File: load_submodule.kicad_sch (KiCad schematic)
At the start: 8 parts, among them Q1 RFP30N06LE

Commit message: Included Shunt Values
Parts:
- added C8: 220uF, symbol Device:C_US
- added Q2: 2N2219, Package_TO_SOT_THT:TO-39-3, symbol Transistor_BJT:2N2219
- added R13: 220, symbol Device:R
- added R14: 470, symbol Device:R
- added R15, R16: R, symbol Device:R
- added R17: 10, symbol Device:R
- added RE1: Relay, symbol windTurbineSchemSymLib:Relay
- added U1, U2: INA229AQDGSRQ1, VSSOP10_DGS_TEX, symbol INA229:INA229AQDGSRQ1
- C5: value C_US -> 100uF
- C6: value C_US -> 22uF
- C7: value C_US -> 220uF
- L1, L2: value L -> 150u
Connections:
- net Converter_Out: now also RE1.5 (COM)
- net GND: now also BT1.2 (-), C8.2, Q2.1 (E), R17.2, RE1.3 (GND), U1.7 (GND), U2.7 (GND)
- net MCU: now also R14.1
- net Rectifier+: now also R16.1, U2.10 (IN+), U2.8 (VBUS); no longer C5.1, L1.1
- net at BT1.1 (+): now also R15.2, U1.9 (IN)
- new net: Q2.3 (C), R13.2, RE1.2 (IN)
- new net: Q2.2 (B), R14.2
- new net: R15.1, RE1.6 (NO), U1.10 (IN+)
- new net +3.3V: C8.1, U1.6 (VS), U2.6 (VS)
- new net +5V: R13.1, RE1.1 (Vcc)
- new net Battery+: U1.8 (VBUS)
- new net Battery_Alert: U1.3 (ALERT)
- new net Battery_CS: U1.1 (CS)
- new net Battery_MISO: U1.4 (MISO)
- new net Battery_MOSI: U1.2 (MOSI)
- new net Battery_SCLK: U1.5 (SCLK)
- new net Converter_In: C5.1, L1.1, R16.2, U2.9 (IN)
- new net Dump_Load: R17.1, RE1.4 (NC)
- new net Rectifier_ALERT: U2.3 (ALERT)
- new net Rectifier_CS: U2.1 (CS)
- new net Rectifier_MISO: U2.4 (MISO)
- new net Rectifier_MOSI: U2.2 (MOSI)
- new net Rectifier_SCLK: U2.5 (SCLK)
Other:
- note added: "100kHz"
- note added: "3.3V"
- note added: "Battery_Shunt"
- note added: "Load Submodule"
- moved on the sheet: BT1, C5, C6, C7, D1, L1, L2, Q1

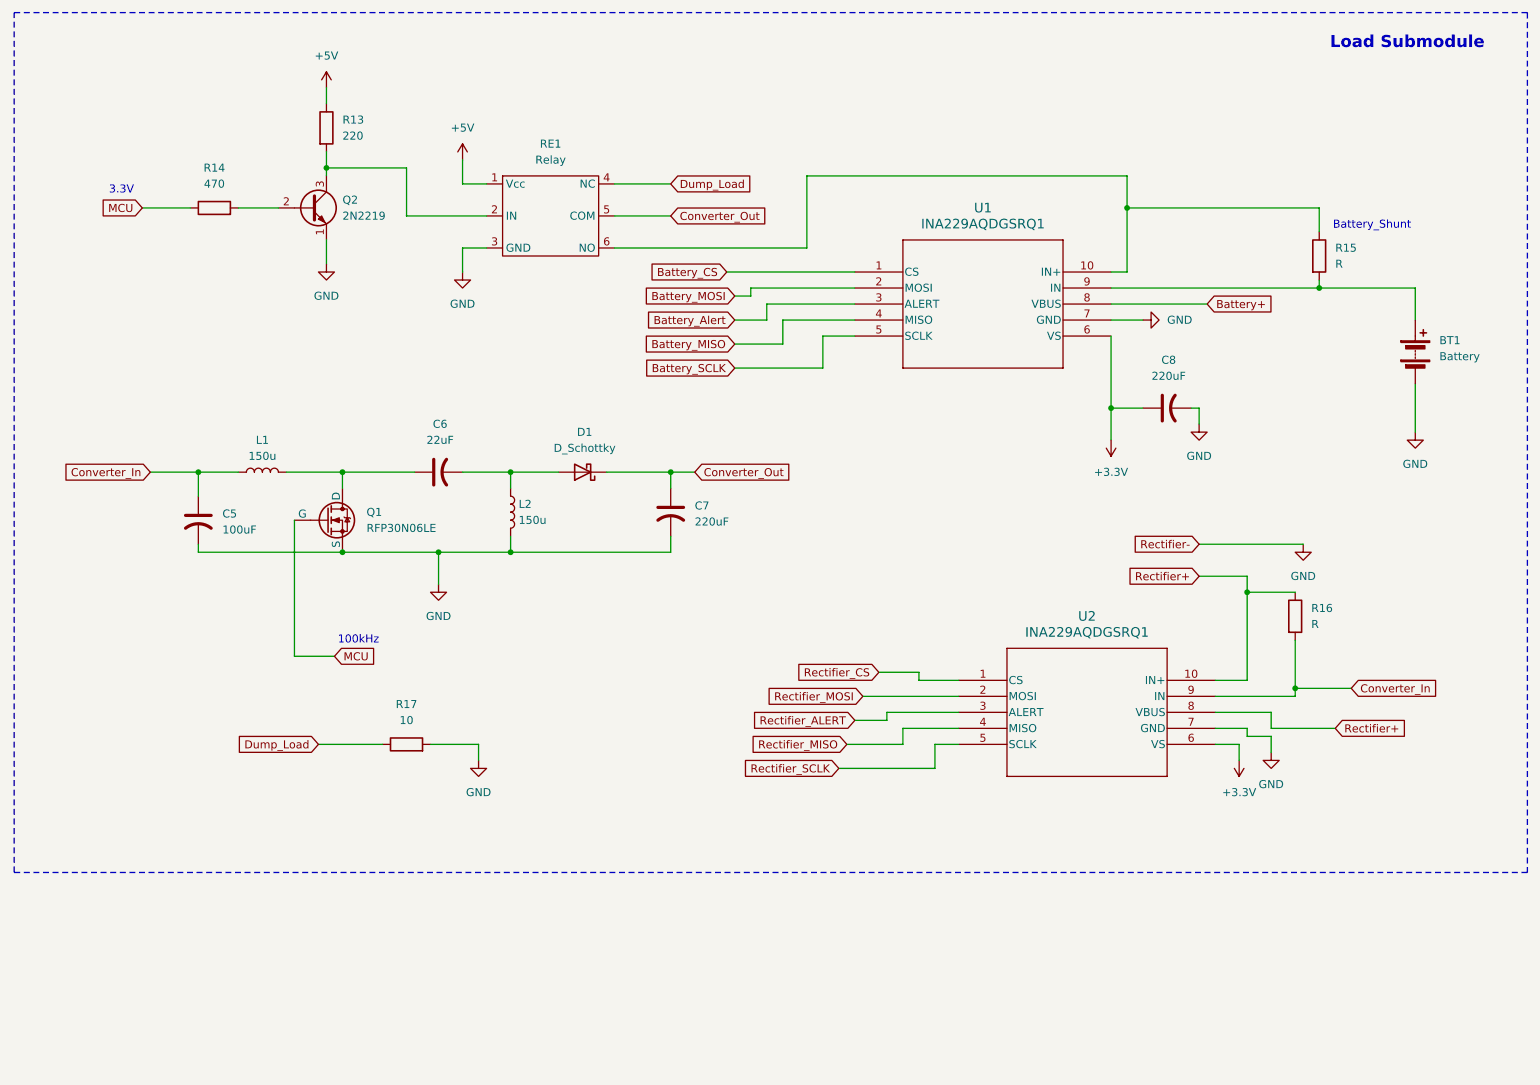
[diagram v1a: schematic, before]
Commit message: Finished Squematics V1
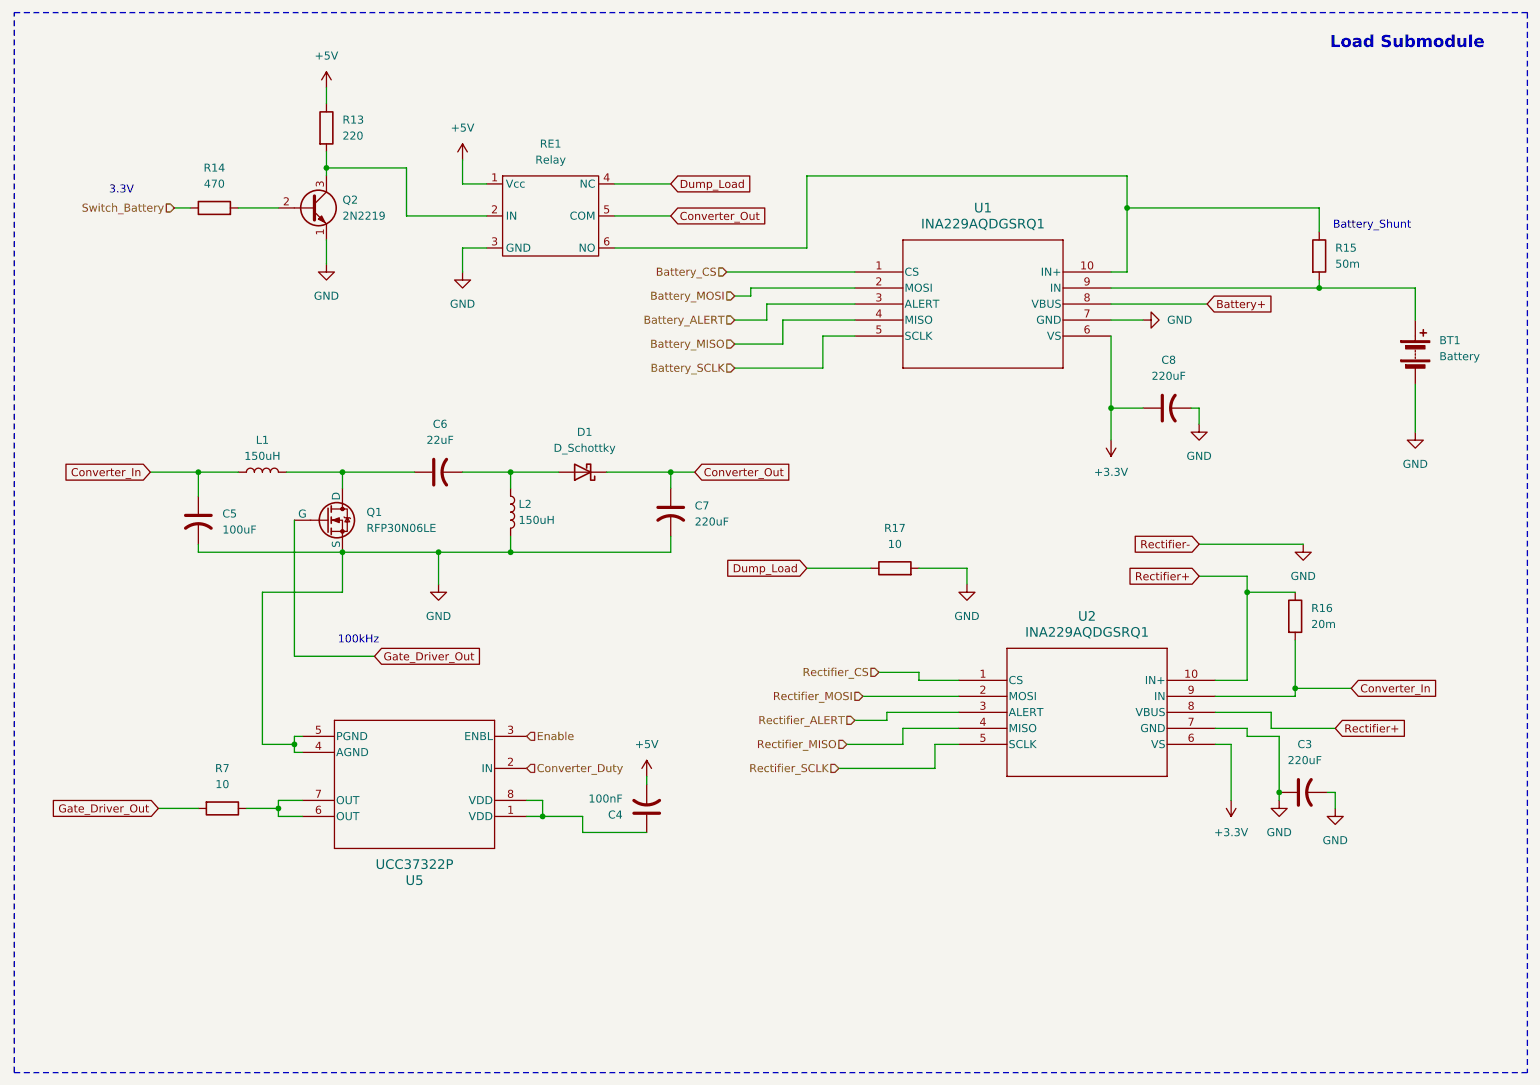
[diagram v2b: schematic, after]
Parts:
- added C3: 220uF, symbol Device:C_US
- added C4: 100nF, symbol Device:C_US
- added R7: 10, symbol Device:R
- added U5: UCC37322P, P0008A, symbol UCC32322:UCC37322P
- L1, L2: value 150u -> 150uH
- R15: value R -> 50m
- R16: value R -> 20m
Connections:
- net +5V: now also C4.2
- net GND: now also C3.1, C3.2, U5.4 (AGND), U5.5 (PGND)
- net Battery_Alert renamed Battery_ALERT
- net MCU renamed Gate_Driver_Out
- net Gate_Driver_Out: now also R7.2; no longer R14.1
- new net: R7.1, U5.6 (OUT), U5.7 (OUT)
- new net: C4.1, U5.1 (VDD), U5.8 (VDD)
- new net Converter_Duty: U5.2 (IN)
- new net Enable: U5.3 (ENBL)
- new net Switch_Battery: R14.1
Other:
- company: (none) -> PRES
- title: (none) -> Load Submodule
- moved on the sheet: R17

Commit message: Added better colors
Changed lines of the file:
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@@
 	)
 	(symbol
+		(lib_name "INA229AQDGSRQ1_1")
 		(lib_id "INA229:INA229AQDGSRQ1")
 		(at 158.75 67.31 0)

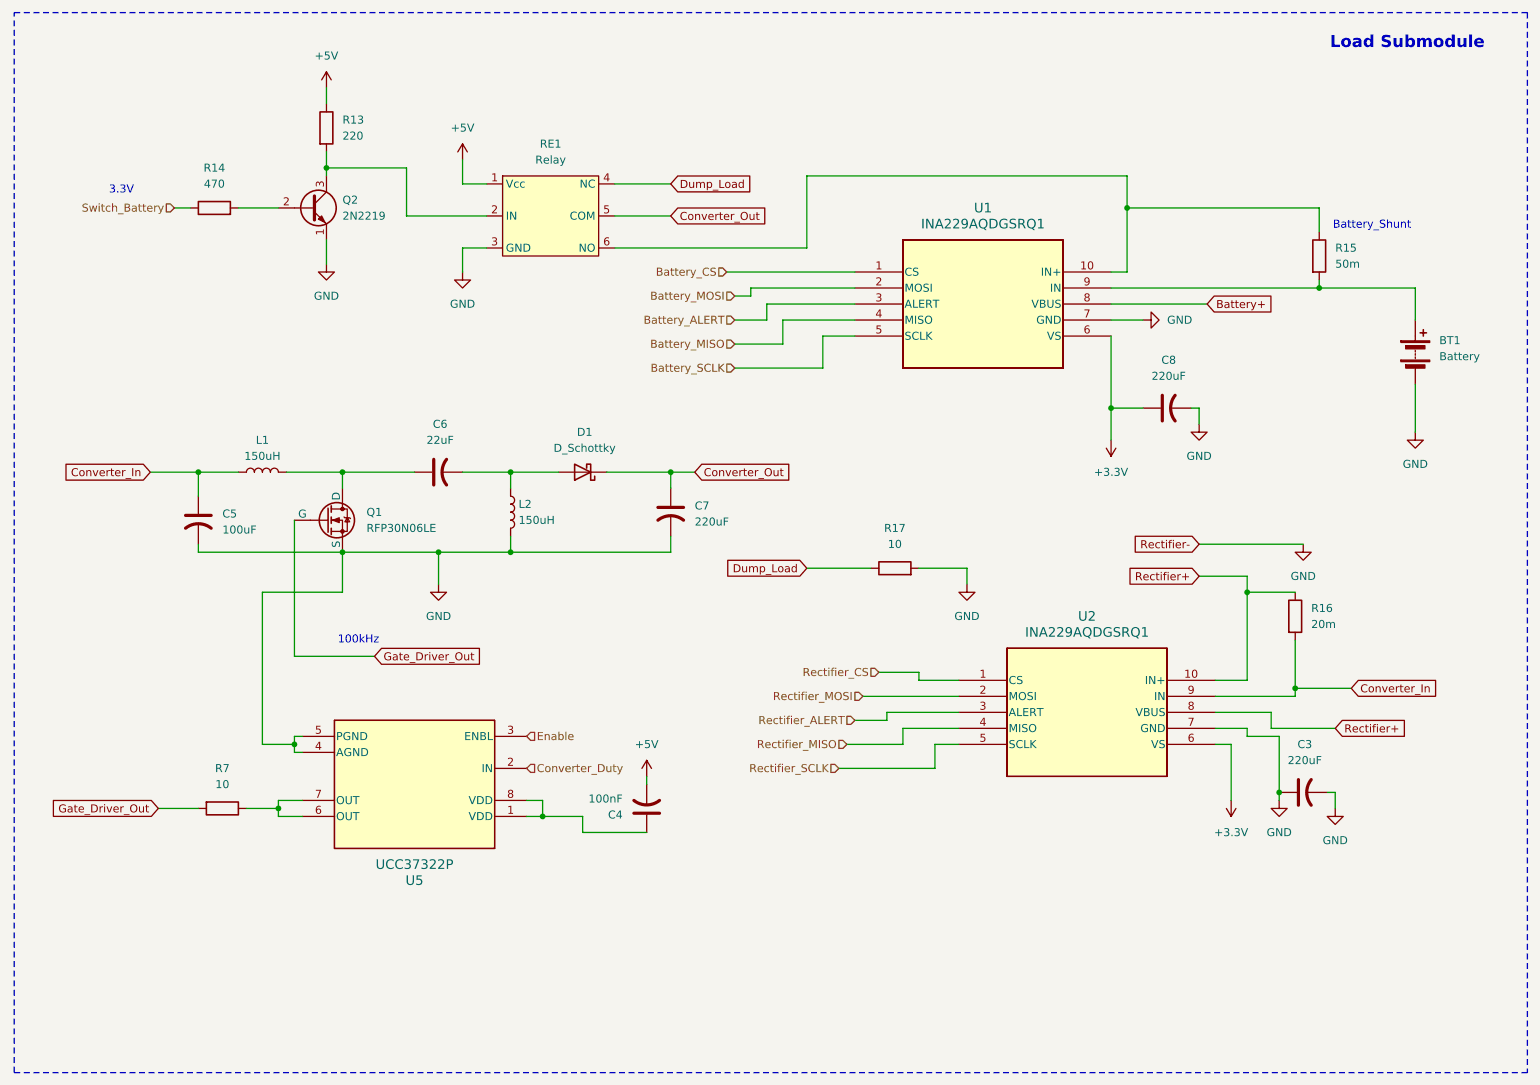
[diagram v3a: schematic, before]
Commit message: converter values adjusted
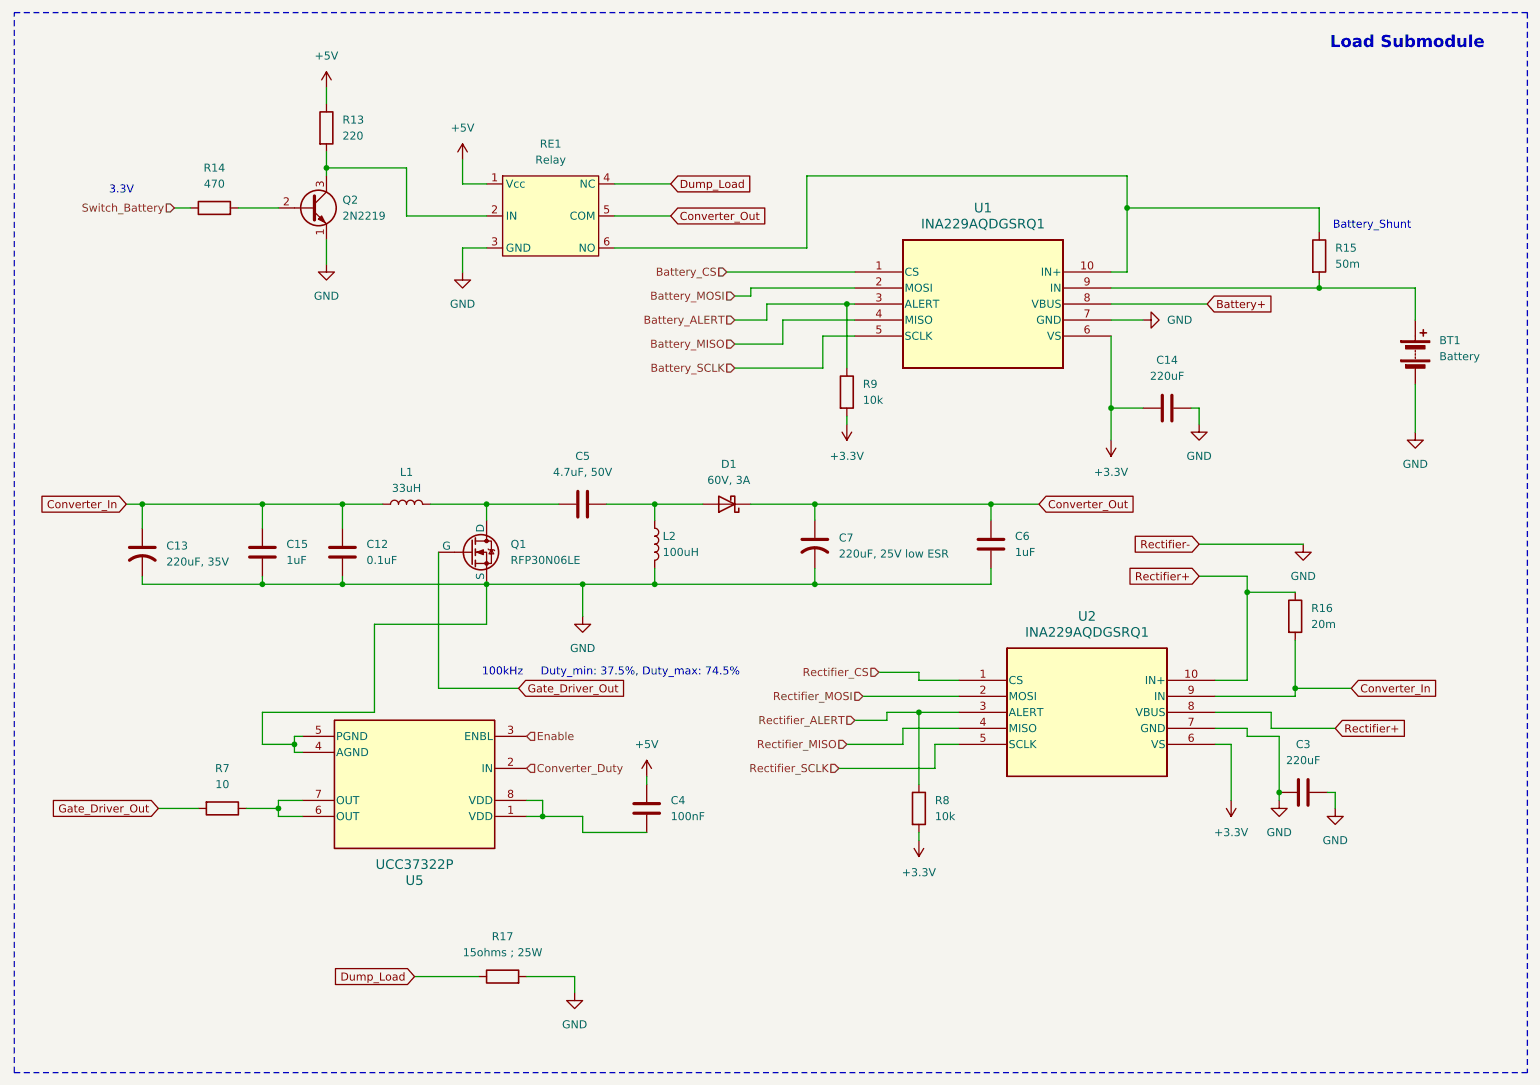
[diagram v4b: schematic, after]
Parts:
- removed C3, C8: 220uF, symbol Device:C_US
- removed C4: 100nF, symbol Device:C_US
- removed C5: 100uF, symbol Device:C_US
- removed C6: 22uF, symbol Device:C_US
- added C12: 0.1uF, symbol Device:C
- added C13: 220uF, 35V, symbol Device:C_US
- added C14, C3: 220uF, symbol Device:C
- added C15, C6: 1uF, symbol Device:C
- added C4: 100nF, symbol Device:C
- added C5: 4.7uF, 50V, symbol Device:C
- added R8, R9: 10k, symbol Device:R
- C7: value 220uF -> 220uF, 25V low ESR
- D1: value D_Schottky -> 60V, 3A
- L1: value 150uH -> 33uH
- L2: value 150uH -> 100uH
- R17: value 10 -> 15ohms ; 25W
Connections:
- net +3.3V: now also C14.1, R8.2, R9.2
- net +5V: now also C4.1
- net Battery_ALERT: now also R9.1
- net Converter_In: now also C12.1, C13.1, C15.1
- net Converter_Out: now also C6.2
- net GND: now also C12.2, C13.2, C14.2, C15.2, C3.1, C3.2, C6.1
- net Rectifier_ALERT: now also R8.1
- net at D1.2 (A), L2.1: now also C5.2
- net at L1.2, Q1.1 (D): now also C5.1
- net at U5.1 (VDD), U5.8 (VDD): now also C4.2
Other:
- note added: "Duty_min: 37.5%, Duty_max: 74.5%"
- moved on the sheet: C7, D1, L1, L2, Q1, R17

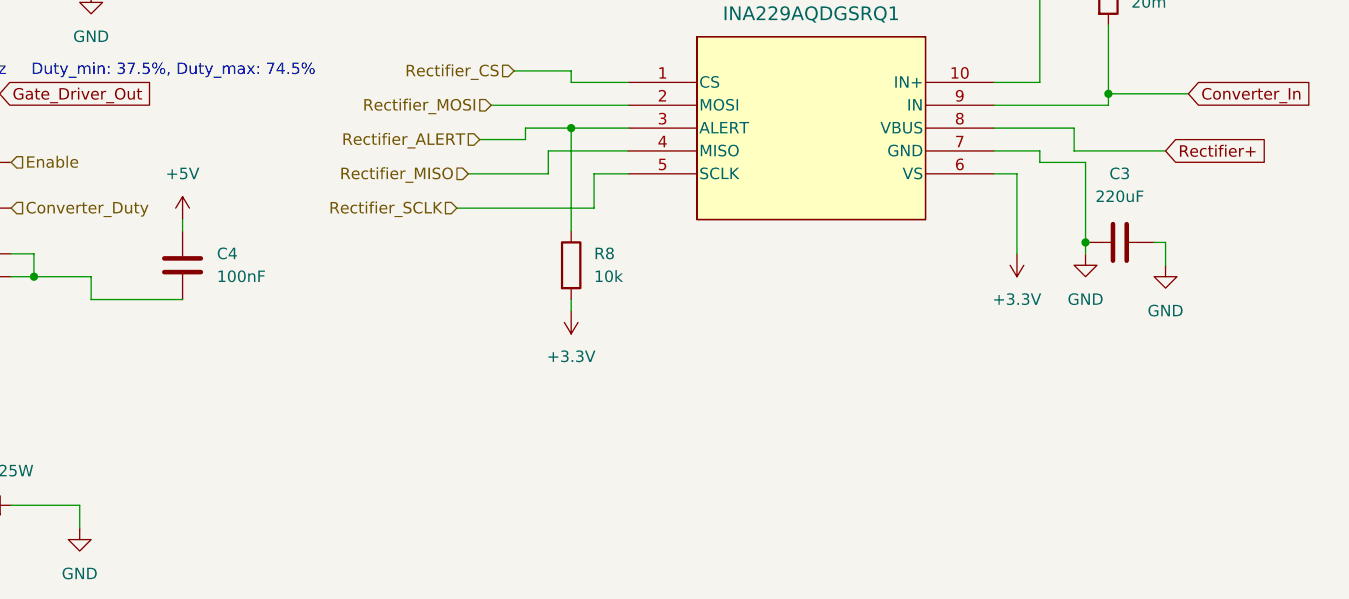
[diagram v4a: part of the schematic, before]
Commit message: Added bypass capacitors, new schmitt trigger IC CMOS compatible
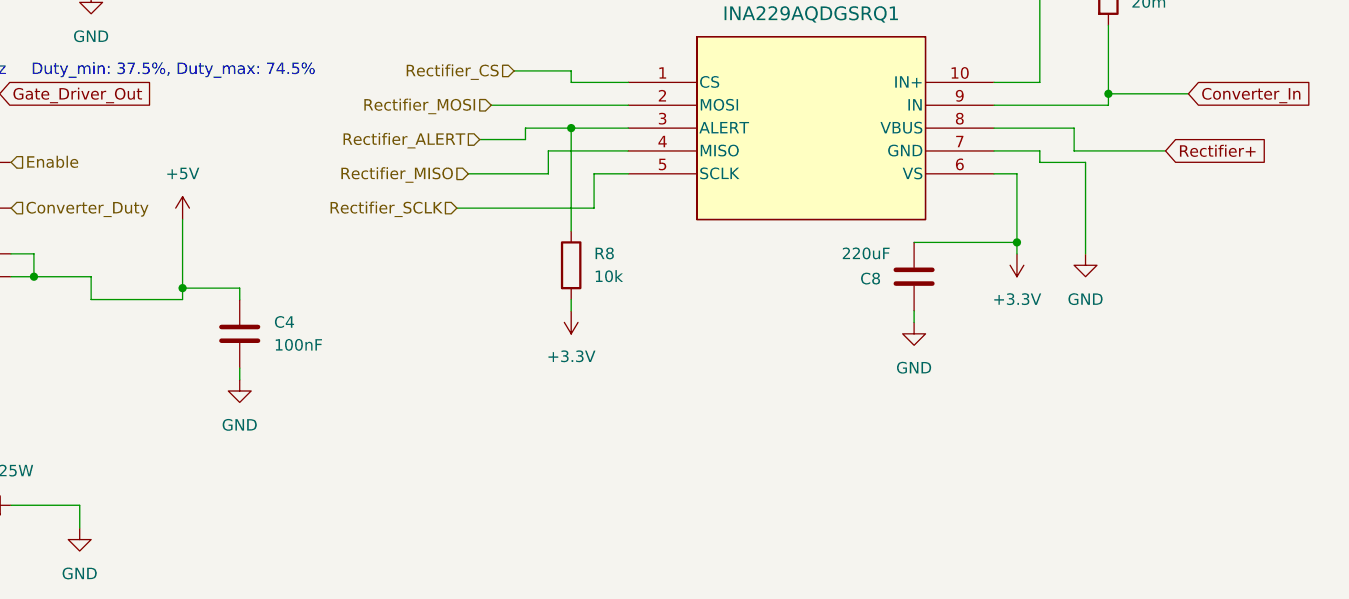
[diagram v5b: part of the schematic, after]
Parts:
- removed C3: 220uF, symbol Device:C
- added C8: 220uF, symbol Device:C
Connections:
- net +3.3V: now also C8.1
- net +5V: now also U5.1 (VDD), U5.8 (VDD)
- net GND: now also C4.2, C8.2
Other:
- moved on the sheet: C4
